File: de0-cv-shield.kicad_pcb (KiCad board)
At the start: 2 copper layers, 88.9 x 78.7 mm, 112 parts, among them P101 USB_OTG, P102 CONN_02X20, Q401 IRF540N, Q402 IRF540N, Q403 IRF540N, Q404 IRF540N, Q405 IRF540N, Q406 IRF540N, U101 ISL89410, U102 ISL89410, U103 FT230XS, U104 STM32F373CCTx, U105 MCP2562-E/SN, U106 LD1117S33TR, U107 MAX9924, U201 LM324, U301 LM324, U501 LM2576xx

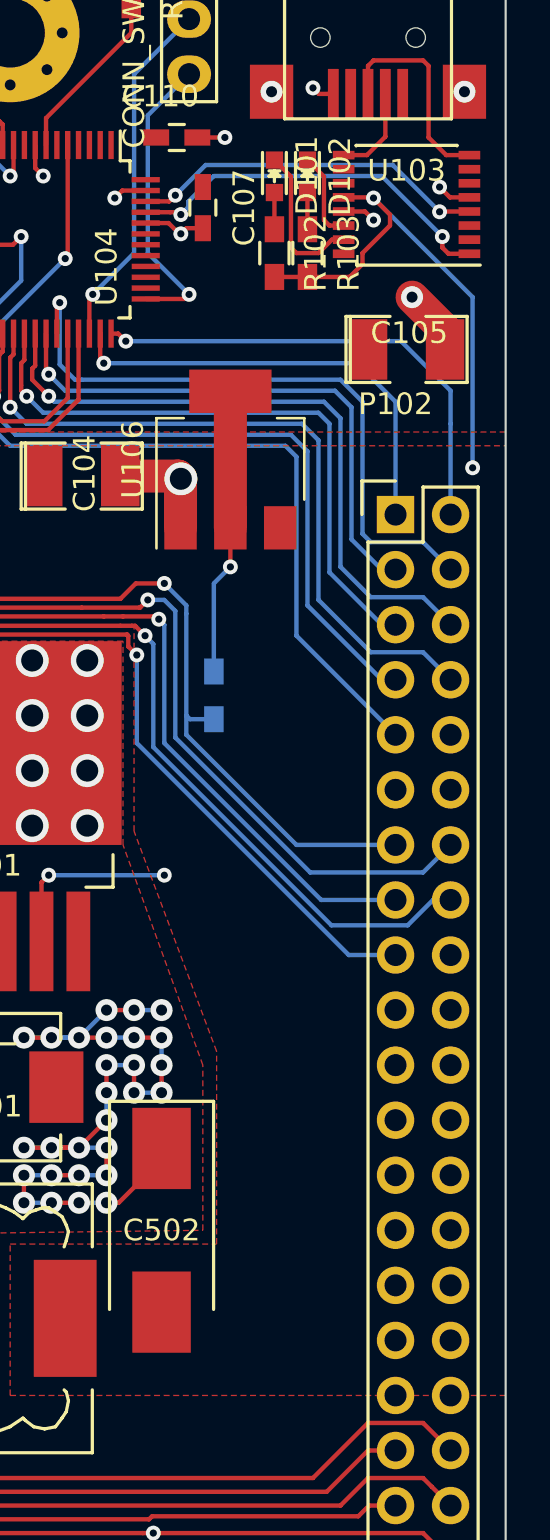
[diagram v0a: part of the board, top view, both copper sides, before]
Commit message: Fix wrong FTDI wiring, add silk board label
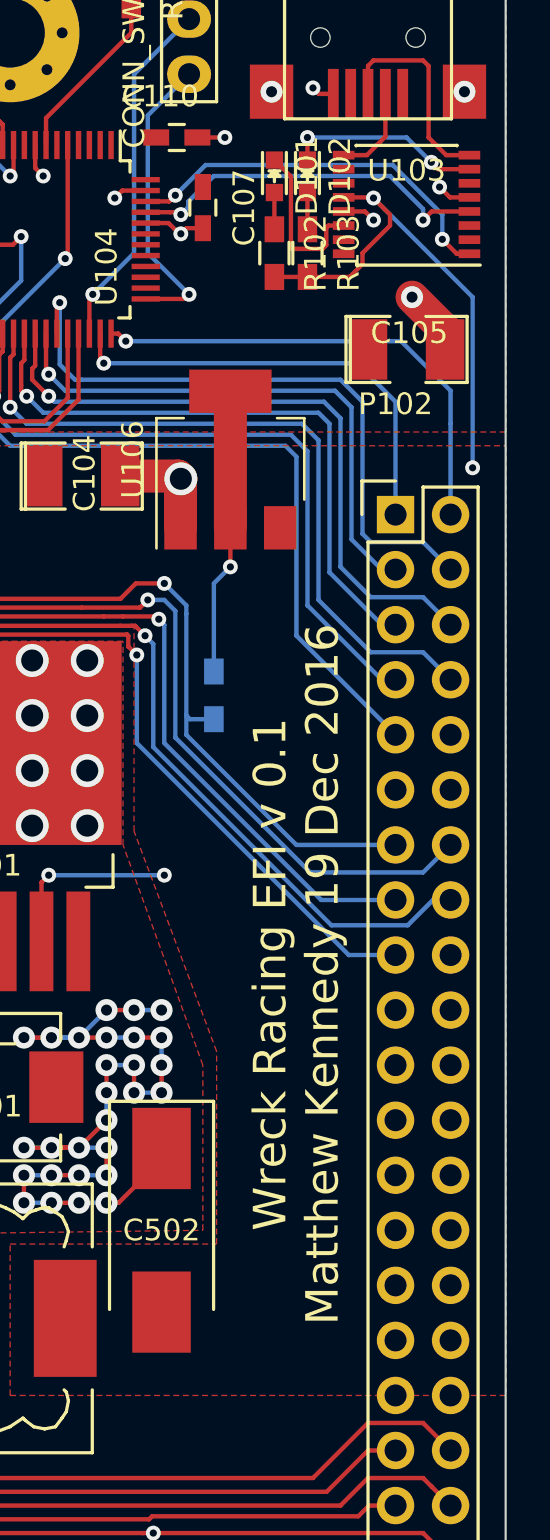
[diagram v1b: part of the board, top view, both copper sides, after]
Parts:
- added REF***: KiCad-Logo2_12mm_SilkScreen, Symbols:KiCad-Logo2_12mm_SilkScreen, B.Cu at (137.5, 119.4)
- added REF***: OSHW-Logo_11.4x12mm_SilkScreen, Symbols:OSHW-Logo_11.4x12mm_SilkScreen, B.Cu at (128.8, 105.3)
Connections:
- U103 pad 14: Net-(D102-Pad1) -> Net-(D101-Pad1)
- U103 pad 15: Net-(D101-Pad1) -> Net-(U103-Pad15)
- U103 pad 7: Net-(U103-Pad7) -> Net-(D102-Pad1)
- U104 pad 45: ftdi_tx -> ftdi_rx
- U104 pad 46: ftdi_rx -> ftdi_tx
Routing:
- net Net-(D102-Pad1): track 4.10 -> 9.12 mm, vias 0 -> 2
- net ftdi_rx: track 16.5 -> 17.2 mm
- net Net-(D101-Pad1): track 7.15 -> 7.72 mm
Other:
- board text added: "Wreck Racing EFI v 0.1 Matthew Kennedy 19 Dec 2016"
